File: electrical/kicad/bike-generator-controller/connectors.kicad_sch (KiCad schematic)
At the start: 0 parts

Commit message: feat: integrate controller modules and schematics
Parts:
- added J2: J_DISPLAY_I2C, Connector_PinHeader_2.54mm:PinHeader_1x04_P2.54mm_Vertical, symbol Connector_Generic:Conn_01x04
- added J3: J_DEBUG_UART, Connector_PinHeader_2.54mm:PinHeader_1x04_P2.54mm_Vertical, symbol Connector_Generic:Conn_01x04
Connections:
- new net +3V3: J2.1 (Pin_1), J3.1 (Pin_1)
- new net GND: J2.2 (Pin_2), J3.2 (Pin_2)
- new net I2C_SCL: J2.4 (Pin_4)
- new net I2C_SDA: J2.3 (Pin_3)
- new net UART_RX: J3.4 (Pin_4)
- new net UART_TX: J3.3 (Pin_3)
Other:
- note added: "J2 DISPLAY I2C: 1=3V3, 2=GND, 3=SDA, 4=SCL"
- note added: "J3 DEBUG UART: 1=3V3, 2=GND, 3=TX (MCU), 4=RX (MCU)"

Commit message: wip: checkpoint controller routing before review
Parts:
- removed J3: J_DEBUG_UART, Connector_PinHeader_2.54mm:PinHeader_1x04_P2.54mm_Vertical, symbol Connector_Generic:Conn_01x04
- added J5: J_EXT_GPIO, Connector_JST:JST_PH_S4B-PH-K_1x04_P2.00mm_Horizontal, symbol Connector_Generic:Conn_01x04
- added R10, R9: 1k, Resistor_SMD:R_0805_2012Metric_Pad1.20x1.40mm_HandSolder, symbol Device:R
- added R7, R8: 10k, Resistor_SMD:R_0805_2012Metric_Pad1.20x1.40mm_HandSolder, symbol Device:R
- renumbered J2 to J3
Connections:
- net +3V3: now also J5.2 (Pin_2), R7.1, R8.1
- net GND: now also J5.1 (Pin_1)
- new net: J5.3 (Pin_3), R9.2
- new net: J5.4 (Pin_4), R10.2
- new net GPIO4_HALL: R8.2, R9.1
- new net GPIO8_ACTION: R10.1, R7.2

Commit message: feat: close controller v1 design and define integrated v2
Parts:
- J5: MPN (none) -> S4B-PH-K-S(LF)(SN); Manufacturer (none) -> JST; Mating Housing (none) -> PHR-4
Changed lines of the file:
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@@
 			)
 		)
-		(property "Datasheet" ""
+		(property "Datasheet" "https://www.jst-mfg.com/product/pdf/eng/ePH.pdf"
 			(at 143.51 123.19 0)
 			(hide yes)
@@
 			(at 143.51 123.19 0)
 			(hide yes)
+			(show_name no)
+			(do_not_autoplace no)
+			(effects
+				(font
+					(size 1.27 1.27)
+				)
+			)
+		)
+		(property "Manufacturer" "JST"
+			(at 143.51 123.19 0)
+			(hide yes)
+			(show_name no)
+			(do_not_autoplace no)
+			(effects
+				(font
+					(size 1.27 1.27)
+				)
+			)
+		)
+		(property "MPN" "S4B-PH-K-S(LF)(SN)"
+			(at 143.51 123.19 0)
+			(hide yes)
+			(show_name no)
+			(do_not_autoplace no)
+			(effects
+				(font
+					(size 1.27 1.27)
+				)
+			)
+		)
+		(property "Mating Housing" "PHR-4"
+			(at 143.51 123.19 0)
+			(hide yes)

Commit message: feat(pcb): finalize V1 controller layout
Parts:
- J5: footprint Connector_JST:JST_PH_S4B-PH-K_1x04_P2.00mm_Horizontal -> Connector_PinHeader_2.54mm:PinHeader_1x04_P2.54mm_Vertical; MPN S4B-PH-K-S(LF)(SN) -> PinHeader_1x04_P2.54mm_THT; Manufacturer JST -> Generic; Mating Housing PHR-4 -> (none)
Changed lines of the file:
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@@
 			)
 		)
-		(property "Footprint" "Connector_JST:JST_PH_S4B-PH-K_1x04_P2.00mm_Horizontal"
+		(property "Footprint" "Connector_PinHeader_2.54mm:PinHeader_1x04_P2.54mm_Vertical"
 			(at 143.51 123.19 0)
 			(hide yes)
@@
 			)
 		)
-		(property "Datasheet" "https://www.jst-mfg.com/product/pdf/eng/ePH.pdf"
+		(property "Datasheet" ""
 			(at 143.51 123.19 0)
 			(hide yes)
@@
 			)
 		)
-		(property "Description" "Generic connector, single row, 01x04, script generated (kicad-library-utils/schlib/autogen/connector/)"
+		(property "Description" "1x4 male pin header, 2.54 mm pitch, vertical, THT"
 			(at 143.51 123.19 0)
 			(hide yes)
@@
 			)
 		)
-		(property "Manufacturer" "JST"
+		(property "Manufacturer" "Generic"
 			(at 143.51 123.19 0)
 			(hide yes)
@@
 			)
 		)
-		(property "MPN" "S4B-PH-K-S(LF)(SN)"
+		(property "MPN" "PinHeader_1x04_P2.54mm_THT"
 			(at 143.51 123.19 0)
 			(hide yes)
@@
 			)
 		)
-		(property "Mating Housing" "PHR-4"
+		(property "Mating Housing" ""
 			(at 143.51 123.19 0)
 			(hide yes)

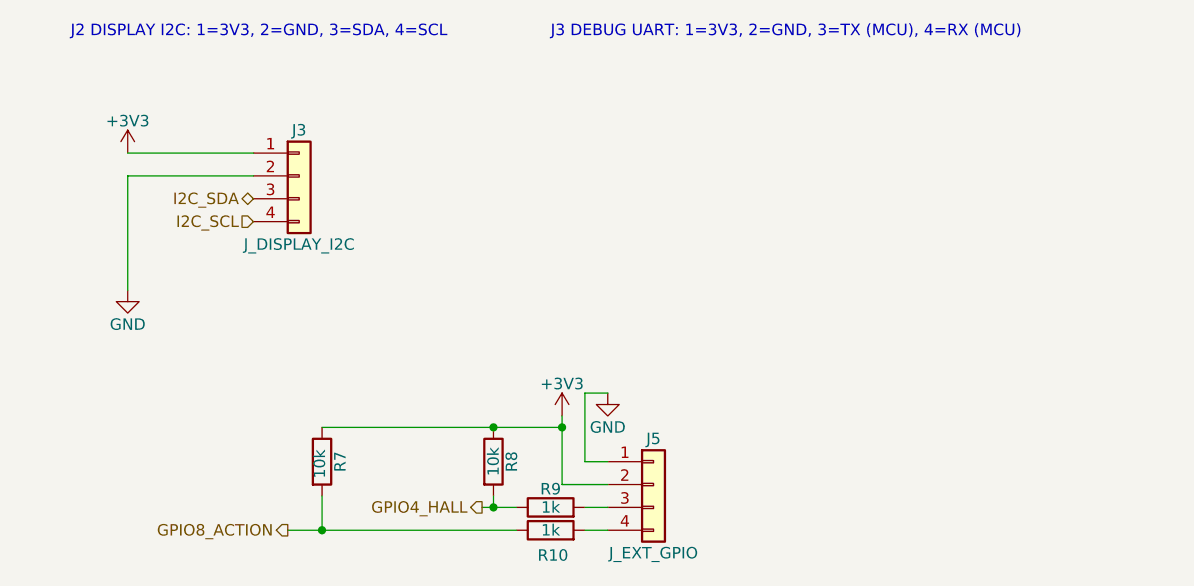
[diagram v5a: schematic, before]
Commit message: feat(controller): finalize V1 design and sourcing
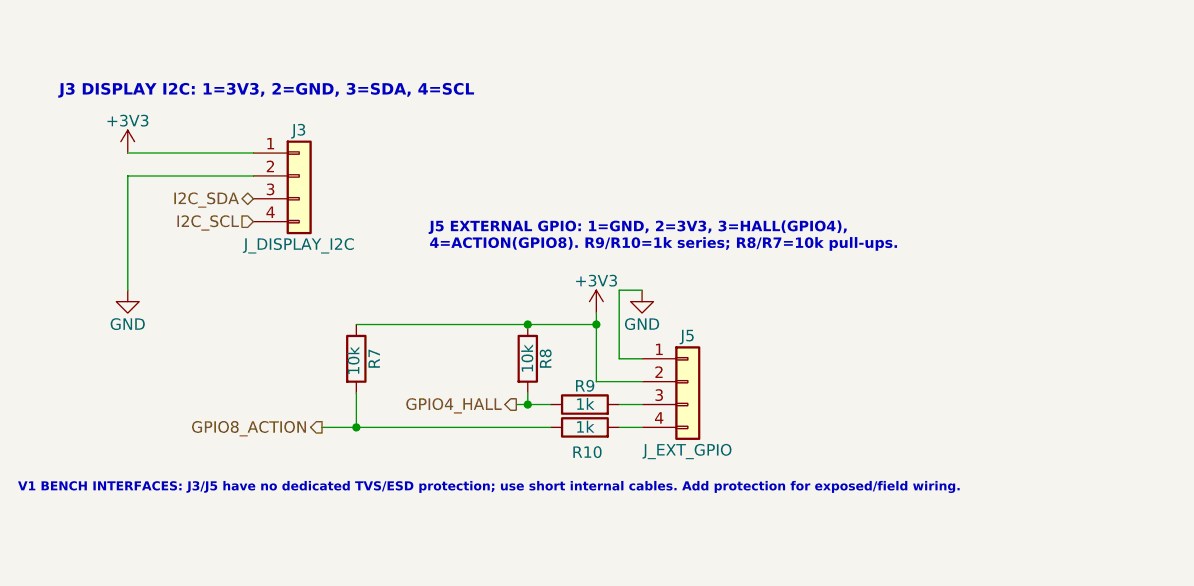
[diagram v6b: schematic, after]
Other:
- note added: "J3 DISPLAY I2C: 1=3V3, 2=GND, 3=SDA, 4=SCL"
- note added: "J5 EXTERNAL GPIO: 1=GND, 2=3V3, 3=HALL(GPIO4), 4=ACTION(GPIO8). R9/R10=1k series; R8/R7=10k pull-ups."
- note added: "V1 BENCH INTERFACES: J3/J5 have no dedicated TVS/ESD protection; use short internal cables. Add protection for exposed/field wiring."
- note removed: "J2 DISPLAY I2C: 1=3V3, 2=GND, 3=SDA, 4=SCL"
- note removed: "J3 DEBUG UART: 1=3V3, 2=GND, 3=TX (MCU), 4=RX (MCU)"
- moved on the sheet: J5, R10, R7, R8, R9
